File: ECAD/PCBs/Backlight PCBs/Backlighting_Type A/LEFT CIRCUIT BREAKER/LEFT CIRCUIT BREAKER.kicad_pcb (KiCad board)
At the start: 2 copper layers, 99.5 x 27 mm, 31 parts, among them J1 Conn_01x04_Female, J2 Conn_01x04_Female

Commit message: Drawing Sheet & Silkscreen update - Backlight Panels (Fc thru Spin)
1:  Updated/Relinked Drawing Sheet for both PCB and Schematics
2:  Standardized Silkscreen (if required)

Finished Remaining Backlighting Type A & Type B PCBs.....
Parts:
- added ?: LOGO, OH_Footprints:OH_LOGO_37.7mm_5.9mm, B.Cu at (165.2, 68.2)
- added ?: LOGO, OH_Footprints:CC-BY-NC-SA-Small, B.Cu at (126.4, 68.5)
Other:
- board text added: "LEFT CIRCUIT BREAKER Revision: 1 www.openhornet.com"

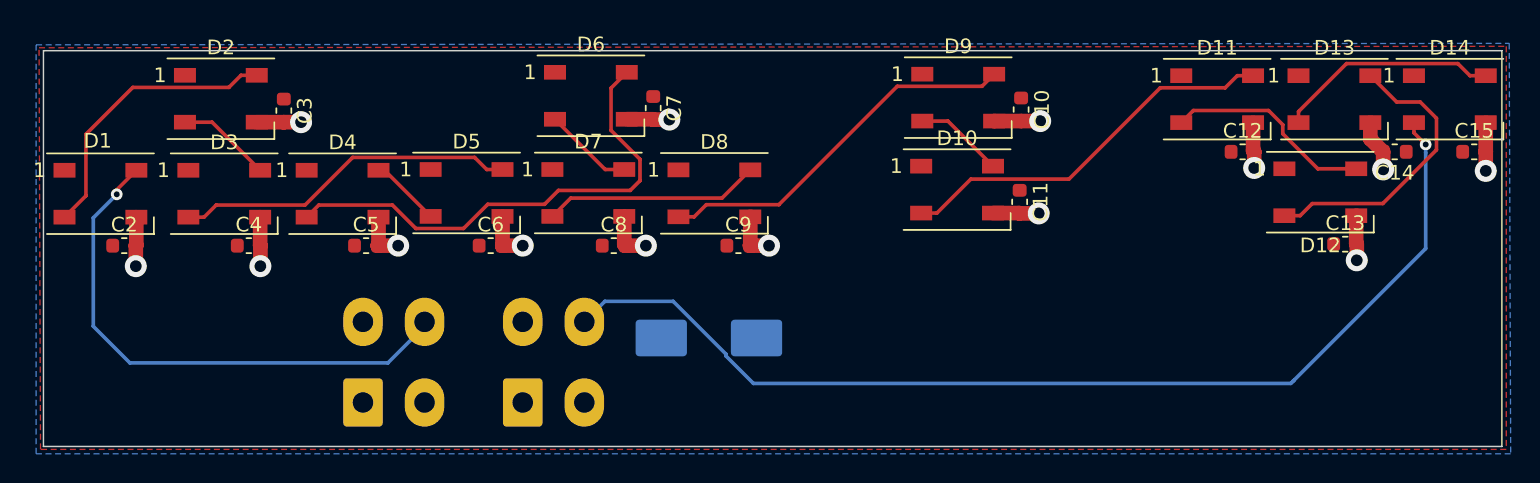
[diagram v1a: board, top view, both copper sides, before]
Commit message: Review: LEFT CB thru OBOGS 100%
Reviewed/adjusted silkscreens as needed
Relinked footprints
Updated Manufacturing files
Updated PNGs and STEP files as needed.
Renamed PNGs for standardization
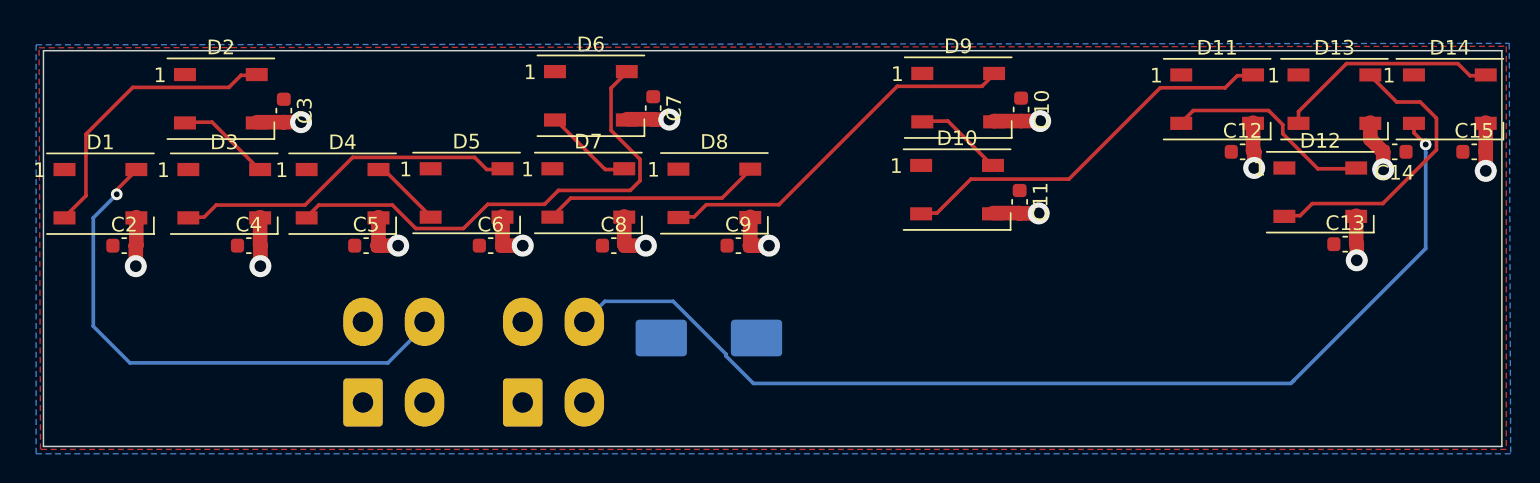
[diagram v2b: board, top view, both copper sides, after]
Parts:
- C1: footprint Capacitor_SMD:CP_Elec_8x10 -> OH_Footprints:CP_Elec_8x10
- C10, C11, C12, C13, C14, C15, C2, C3, C4, C5, C6, C7, C8, C9: footprint Capacitor_SMD:C_0603_1608Metric -> OH_Footprints:C_0603_1608Metric
- D1, D10, D11, D12, D13, D14, D2, D3, D4, D5, D6, D7, D8, D9: footprint LED_SMD:LED_WS2812B_PLCC4_5.0x5.0mm_P3.2mm -> OH_Footprints:LED_WS2812B_PLCC4_5.0x5.0mm_P3.2mm
- J1, J2: footprint Connector_Molex:Molex_Mini-Fit_Jr_5566-04A_2x02_P4.20mm_Vertical -> OH_Footprints:Molex_Mini-Fit_Jr_5566-04A_2x02_P4.20mm_Vertical

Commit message: KiCad 7 Transition - LEFT CIRCUIT BREAKER
PCB and Schematic standardization
Updated silkscreen text
Adjusted traces to prevent conflicts
Add Testpoints
Recompiled assets and manufacturing files

**Labeled the Left Circuit Breaker as "Revision 4" to bring it up to speed with everything else.  The PCB silkscreen had Revision 1, the schematic said 3, and a previous BOM showed it as 2.2(?).  Figured it best to keep everything level across the board as a starting point to keep track of future changes.
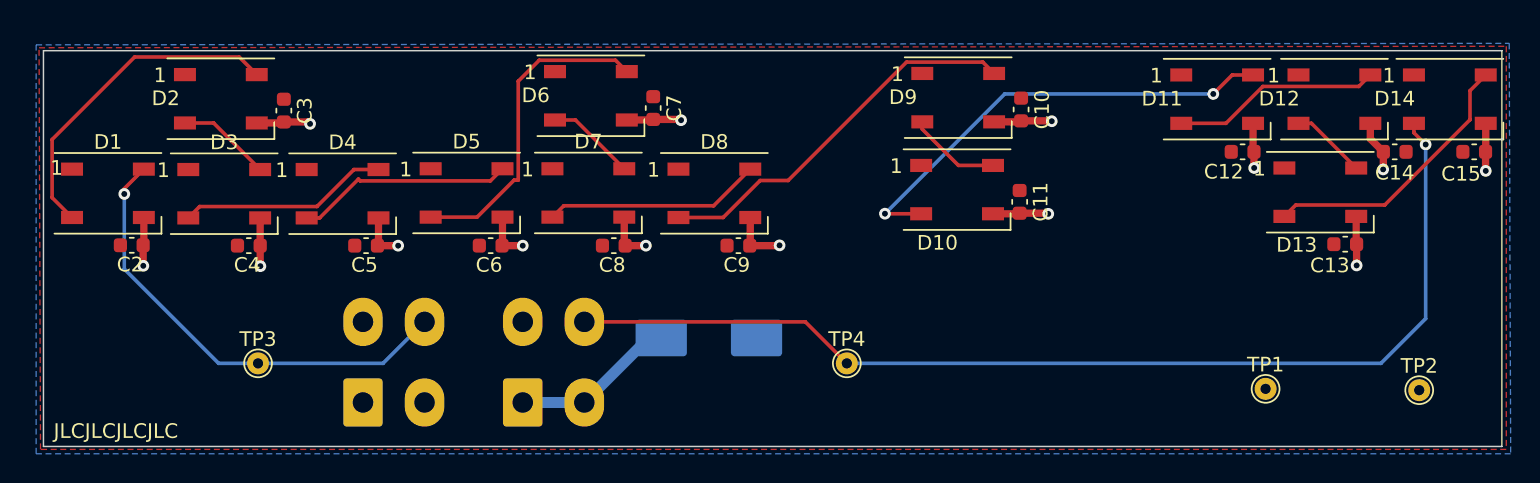
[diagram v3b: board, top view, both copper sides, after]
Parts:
- added TP1: TestPoint, OH_Footprints:TestPoint_THTPad_D1.5mm_Drill0.7mm, F.Cu at (183.4, 83.6)
- added TP2: TestPoint, OH_Footprints:TestPoint_THTPad_D1.5mm_Drill0.7mm, F.Cu at (193.9, 83.7)
- added TP3: TestPoint, OH_Footprints:TestPoint_THTPad_D1.5mm_Drill0.7mm, F.Cu at (114.6, 81.8)
- added TP4: TestPoint, OH_Footprints:TestPoint_THTPad_D1.5mm_Drill0.7mm, F.Cu at (154.8, 81.8)
- C1: value C_Polarized -> 1000uF
- C10, C11, C12, C13, C14, C15, C2, C3, C4, C5, C6, C7, C8, C9: value C -> 0.1uF
- J1, J2: value Conn_01x04_Female -> Mini-Fit Jr. 2x02
- LOGO1: renamed from ?; footprint OH_Footprints:OH_LOGO_37.7mm_5.9mm -> OH_Footprints:LOGO_OH_Text_Small
- LOGO2: renamed from ?; footprint OH_Footprints:CC-BY-NC-SA-Small -> OH_Footprints:LOGO_CC-BY-NC-SA_Half_Small
- moved LOGO2 53.7 mm to (177.9, 83.6)
- moved LOGO1 4.39 mm to (169.3, 66.7)
- moved D1 0.51 mm to (104.4, 70.2)
- moved C2 0.51 mm to (106.0, 73.8)
- renumbered D13 to D12, D12 to D13
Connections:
- net /DATAIN renamed DATA IN
- net /DATAOUT renamed DATA OUT
- net /LED+5V renamed +5V
- net /LEDGND renamed GND
- net Net-(D7-Pad2) renamed /DATA1
- D11 pad 2: Net-(D11-Pad2) -> Net-(D11-DOUT)
- D12 pad 2: Net-(D13-Pad2) -> Net-(D12-DOUT)
- D12 pad 4: Net-(D12-Pad2) -> Net-(D11-DOUT)
- D13 pad 2: Net-(D12-Pad2) -> Net-(D13-DOUT)
- D13 pad 4: Net-(D11-Pad2) -> Net-(D12-DOUT)
- D14 pad 4: Net-(D13-Pad2) -> Net-(D13-DOUT)
- D3 pad 2: Net-(D3-Pad2) -> Net-(D3-DOUT)
- D4 pad 2: Net-(D4-Pad2) -> Net-(D4-DOUT)
- D4 pad 4: Net-(D4-Pad4) -> Net-(D3-DOUT)
- D5 pad 2: Net-(D4-Pad4) -> Net-(D5-DOUT)
- D5 pad 4: Net-(D3-Pad2) -> Net-(D4-DOUT)
- D6 pad 4: Net-(D4-Pad2) -> Net-(D5-DOUT)
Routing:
- net Net-(D4-Pad2): track 33.8 -> 0.00 mm
- net Net-(D3-Pad2): track 23.5 -> 0.00 mm
- net Net-(D5-DOUT): track 0.00 -> 22.1 mm
- net Net-(D12-Pad2): track 20.1 -> 0.00 mm
- net Net-(D13-DOUT): track 0.00 -> 18.9 mm
- net Net-(D13-Pad2): track 15.2 -> 0.00 mm
- net Net-(D4-DOUT): track 0.00 -> 14.8 mm
- net Net-(D3-DOUT): track 0.00 -> 14.3 mm
- net Net-(D11-Pad2): track 14.3 -> 0.00 mm
- net Net-(D11-DOUT): track 0.00 -> 14.3 mm
- net +5V: track 0.00 -> 10.4 mm
- net Net-(D12-DOUT): track 0.00 -> 5.20 mm
- net DATA IN: track 36.8 -> 31.7 mm
- net Net-(D10-DOUT): track 26.5 -> 31.5 mm, vias 0 -> 2
- net Net-(D4-Pad4): track 4.86 -> 0.00 mm
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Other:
- board text added: "0.2000 mm / 0.0000 mm"
- board text added: "0.3000 mm"
- board text added: "1.6000 mm"
- board text added: "2"
- board text added: "99.5000 mm x 27.0000 mm"
- board text added: "BOARD CHARACTERISTICS"
- board text added: "Board Thickness:"
- board text added: "Board overall dimensions:"
- board text added: "Castellated pads:"
- board text added: "Copper Finish:"
- board text added: "Copper Layer Count:"
- board text added: "Edge card connectors:"
- board text added: "Impedance Control:"
- board text added: "JLCJLCJLCJLC"
- board text added: "LEFT CIRCUIT BREAKER REV: 4 WWW.OPENHORNET.COM"
- board text added: "Min hole diameter:"
- board text added: "Min track/spacing:"
- board text added: "No"
- board text added: "None"
- board text added: "POWER REQUIREMENTS: VOLTAGE: 5V DC LEDS: 14 CURRENT: 0.84A WATTAGE: 4.2W"
- board text added: "Plated Board Edge:"
- board text removed: "LEFT CIRCUIT BREAKER Revision: 1 www.openhornet.com"
